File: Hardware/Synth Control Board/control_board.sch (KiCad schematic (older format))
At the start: 41 parts, among them J1 Conn_01x13, J2 Conn_01x03, J3 Conn_01x13, J4 Conn_01x13, J5 Conn_01x02, J6 Conn_01x13, J7 Conn_01x08, SW1 SW_DPDT_x2, SW10 SW_SPST, SW11 SW_SPST, SW12 SW_SPST, SW13 SW_SPST, SW2 SW_SPST, SW3 SW_SPST, SW4 SW_SPST, SW5 SW_SPST, SW6 SW_SPST, SW7 SW_SPST, SW8 SW_SPST, SW9 SW_SPST

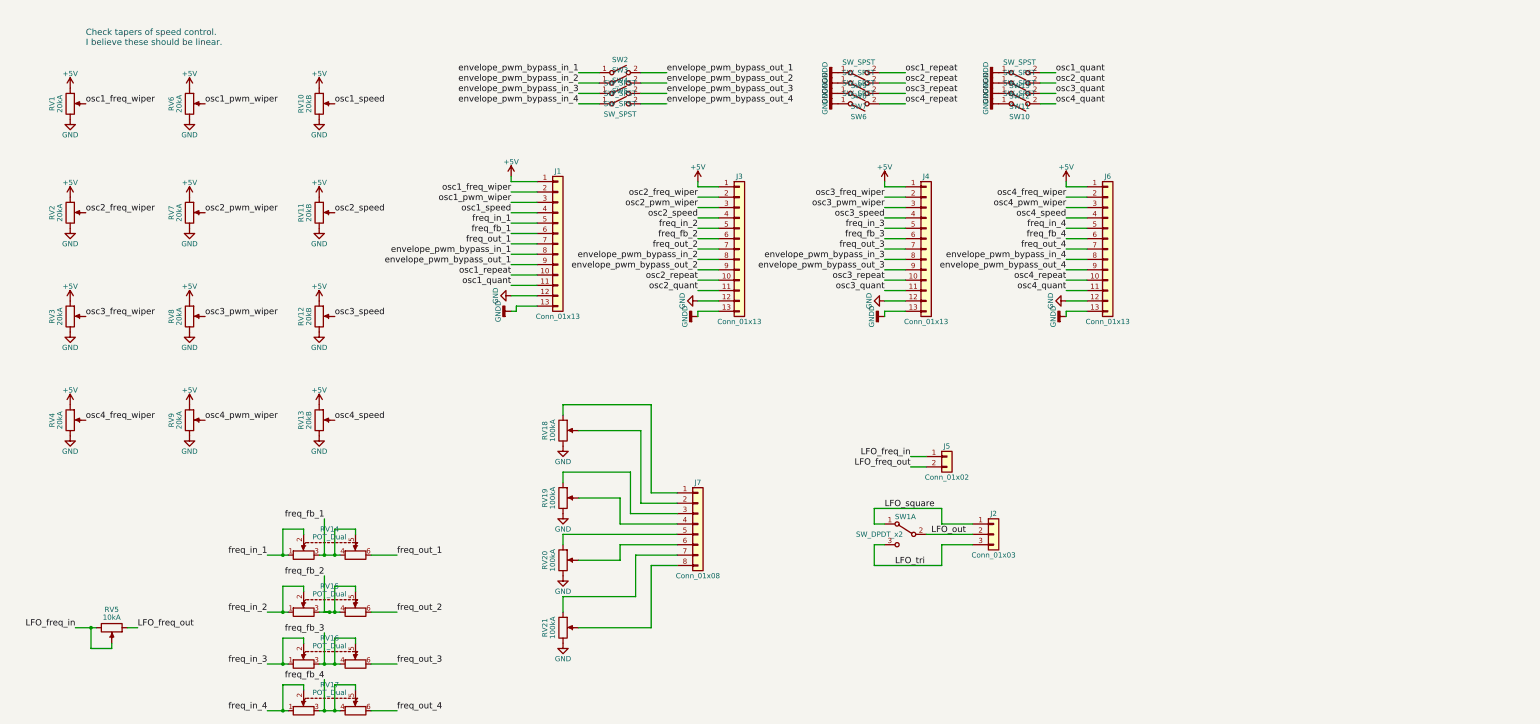
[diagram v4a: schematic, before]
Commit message: add LFO mod pots to control board and fix pot placement
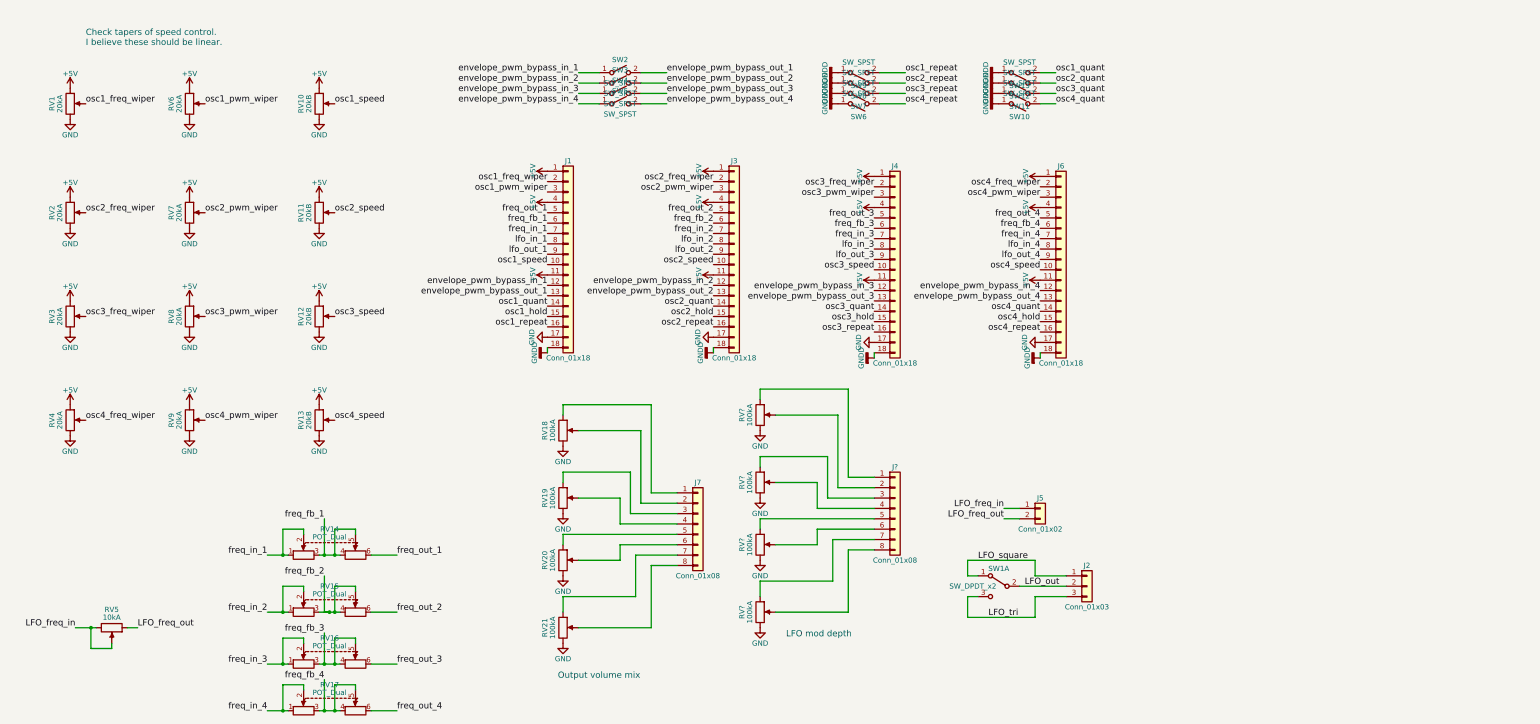
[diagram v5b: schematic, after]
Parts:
- removed J1, J3, J4, J6: Conn_01x13, Pin_Headers:Pin_Header_Straight_1x13_Pitch2.54mm, symbol Conn_01x13
- added J1, J3, J4, J6: Conn_01x18, Pin_Headers:Pin_Header_Straight_1x18_Pitch2.54mm, symbol Conn_01x18
- added J?: Conn_01x08, Pin_Headers:Pin_Header_Straight_1x08_Pitch2.54mm, symbol Conn_01x08
- added RV? (x4): 100kA, Potentiometers:Potentiometer_Bourns_PTV09A-1_Horizontal, symbol POT
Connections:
- net +5V: now also J1.1 (Pin_1), J1.11 (Pin_11), J1.4 (Pin_4), J3.1 (Pin_1), J3.11 (Pin_11), J3.4 (Pin_4), J4.1 (Pin_1), J4.11 (Pin_11), J4.4 (Pin_4), J6.1 (Pin_1), J6.11 (Pin_11), J6.4 (Pin_4)
- net GND: now also J1.17 (Pin_17), J3.17 (Pin_17), J4.17 (Pin_17), J6.17 (Pin_17), RV?.3, RV?.3, RV?.3, RV?.3
- net GNDD: now also J1.18 (Pin_18), J3.18 (Pin_18), J4.18 (Pin_18), J6.18 (Pin_18)
- net envelope_pwm_bypass_in_1: now also J1.12 (Pin_12)
- net envelope_pwm_bypass_in_2: now also J3.12 (Pin_12)
- net envelope_pwm_bypass_in_3: now also J4.12 (Pin_12)
- net envelope_pwm_bypass_in_4: now also J6.12 (Pin_12)
- net envelope_pwm_bypass_out_1: now also J1.13 (Pin_13)
- net envelope_pwm_bypass_out_2: now also J3.13 (Pin_13)
- net envelope_pwm_bypass_out_3: now also J4.13 (Pin_13)
- net envelope_pwm_bypass_out_4: now also J6.13 (Pin_13)
- net freq_fb_1: now also J1.6 (Pin_6)
- net freq_fb_2: now also J3.6 (Pin_6)
- net freq_fb_3: now also J4.6 (Pin_6)
- net freq_fb_4: now also J6.6 (Pin_6)
- net freq_in_1: now also J1.7 (Pin_7)
- net freq_in_2: now also J3.7 (Pin_7)
- net freq_in_3: now also J4.7 (Pin_7)
- net freq_in_4: now also J6.7 (Pin_7)
- net freq_out_1: now also J1.5 (Pin_5)
- net freq_out_2: now also J3.5 (Pin_5)
- net freq_out_3: now also J4.5 (Pin_5)
- net freq_out_4: now also J6.5 (Pin_5)
- net osc1_freq_wiper: now also J1.2 (Pin_2)
- net osc1_pwm_wiper: now also J1.3 (Pin_3)
- net osc1_quant: now also J1.14 (Pin_14)
- net osc1_repeat: now also J1.16 (Pin_16)
- net osc1_speed: now also J1.10 (Pin_10)
- net osc2_freq_wiper: now also J3.2 (Pin_2)
- net osc2_pwm_wiper: now also J3.3 (Pin_3)
- net osc2_quant: now also J3.14 (Pin_14)
- net osc2_repeat: now also J3.16 (Pin_16)
- net osc2_speed: now also J3.10 (Pin_10)
- net osc3_freq_wiper: now also J4.2 (Pin_2)
- net osc3_pwm_wiper: now also J4.3 (Pin_3)
- net osc3_quant: now also J4.14 (Pin_14)
- net osc3_repeat: now also J4.16 (Pin_16)
- net osc3_speed: now also J4.10 (Pin_10)
- net osc4_freq_wiper: now also J6.2 (Pin_2)
- net osc4_pwm_wiper: now also J6.3 (Pin_3)
- net osc4_quant: now also J6.14 (Pin_14)
- net osc4_repeat: now also J6.16 (Pin_16)
- net osc4_speed: now also J6.10 (Pin_10)
- new net: J?.1 (Pin_1), RV?.1
- new net: J?.2 (Pin_2), RV?.2
- new net: J?.3 (Pin_3), RV?.1
- new net: J?.4 (Pin_4), RV?.2
- new net: J?.5 (Pin_5), RV?.1
- new net: J?.6 (Pin_6), RV?.2
- new net: J?.7 (Pin_7), RV?.1
- new net: J?.8 (Pin_8), RV?.2
- new net lfo_in_1: J1.8 (Pin_8)
- new net lfo_in_2: J3.8 (Pin_8)
- new net lfo_in_3: J4.8 (Pin_8)
- new net lfo_in_4: J6.8 (Pin_8)
- new net lfo_out_1: J1.9 (Pin_9)
- new net lfo_out_2: J3.9 (Pin_9)
- new net lfo_out_3: J4.9 (Pin_9)
- new net lfo_out_4: J6.9 (Pin_9)
- new net osc1_hold: J1.15 (Pin_15)
- new net osc2_hold: J3.15 (Pin_15)
- new net osc3_hold: J4.15 (Pin_15)
- new net osc4_hold: J6.15 (Pin_15)
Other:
- note added: "LFO mod depth"
- note added: "Output volume mix"
- moved on the sheet: J2, J5, SW1A

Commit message: route traces to bypass caps on MCU. control board and connectors are WIP.
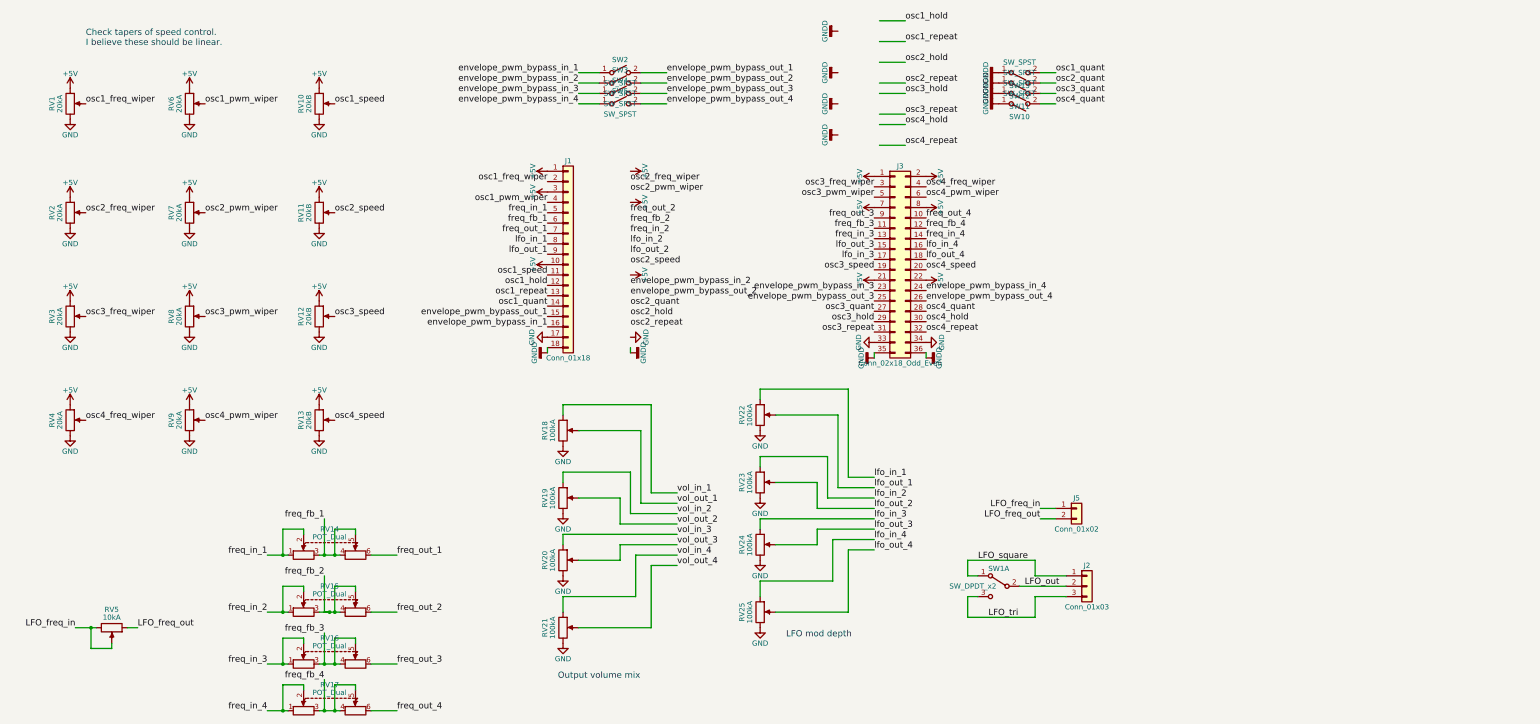
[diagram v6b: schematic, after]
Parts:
- removed J3, J4, J6: Conn_01x18, Pin_Headers:Pin_Header_Straight_1x18_Pitch2.54mm, symbol Conn_01x18
- removed J7, J?: Conn_01x08, Pin_Headers:Pin_Header_Straight_1x08_Pitch2.54mm, symbol Conn_01x08
- removed SW6, SW7, SW8, SW9: SW_SPST, SparkFun-Electromechanical:SWITCH-SPDT, symbol SW_SPST
- added J3: Conn_02x18_Odd_Even, Pin_Headers:Pin_Header_Straight_2x18_Pitch2.54mm, symbol Conn_02x18_Odd_Even
- gave numbers to parts that had none: 4
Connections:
- net labels added: vol_in_1, vol_in_2, vol_in_3, vol_in_4, vol_out_1, vol_out_2, vol_out_3, vol_out_4
- wire segments 131 -> 135
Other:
- moved on the sheet: J5

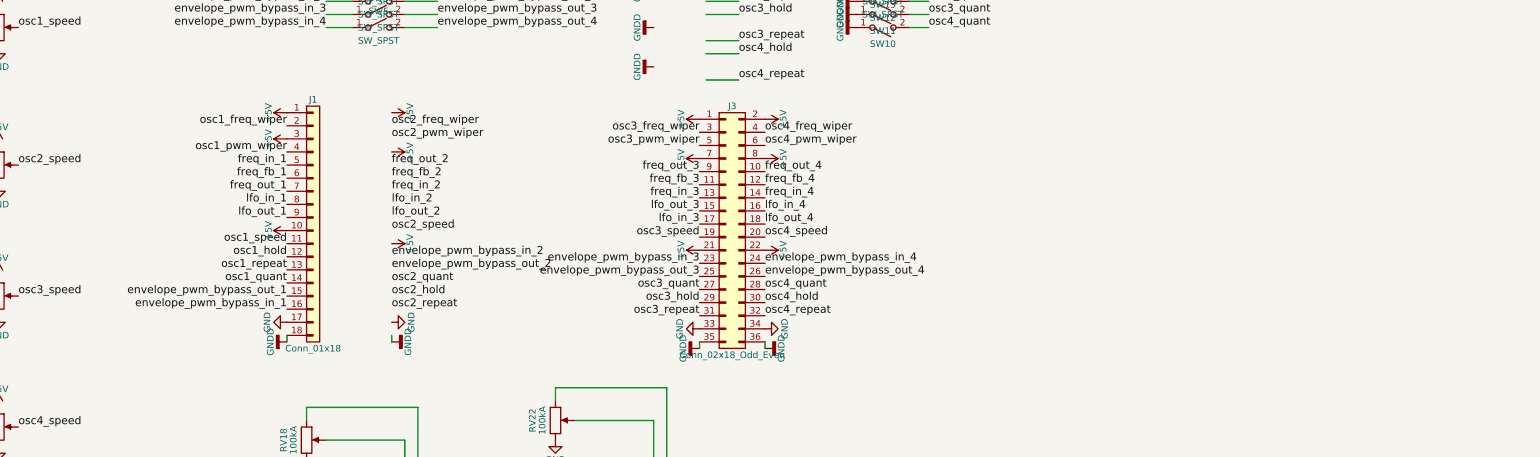
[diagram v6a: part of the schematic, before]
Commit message: route connectors on control board. Will add additional set of connectors for filter knobs to simplify routing.
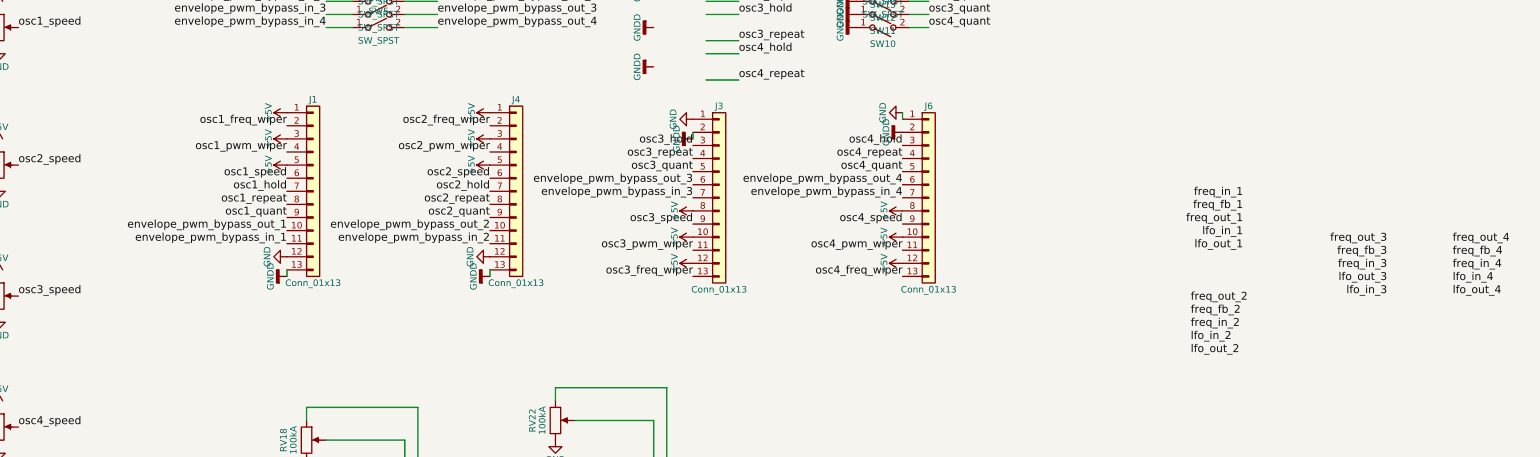
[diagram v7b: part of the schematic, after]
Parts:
- removed J1: Conn_01x18, Pin_Headers:Pin_Header_Straight_1x18_Pitch2.54mm, symbol Conn_01x18
- removed J3: Conn_02x18_Odd_Even, Pin_Headers:Pin_Header_Straight_2x18_Pitch2.54mm, symbol Conn_02x18_Odd_Even
- added J1, J3, J4, J6: Conn_01x13, Pin_Headers:Pin_Header_Straight_1x13_Pitch2.54mm, symbol Conn_01x13

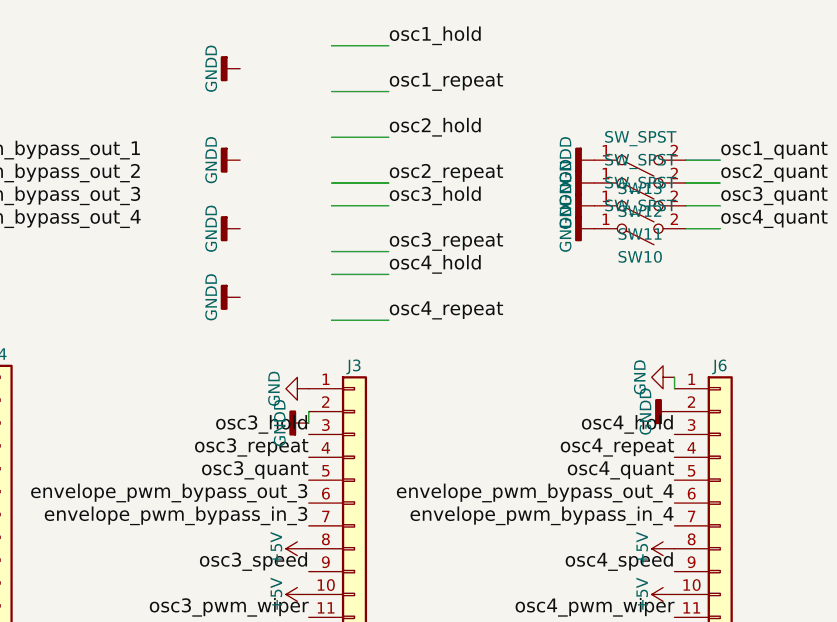
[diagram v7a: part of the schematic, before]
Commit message: fix SPDT hold/repeat switches on control board
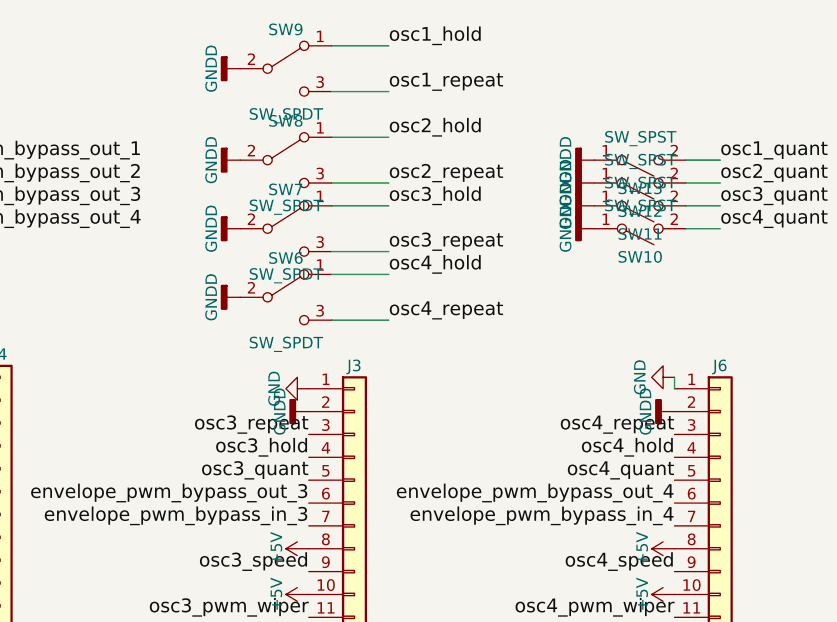
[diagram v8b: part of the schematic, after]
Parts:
- added SW6, SW7, SW8, SW9: SW_SPDT, SparkFun-Electromechanical:SWITCH-SPDT, symbol SW_SPDT
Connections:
- wire segments 135 -> 134
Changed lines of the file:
@@
 Text Label 8800 2500 2    60   ~ 0
 envelope_pwm_bypass_out_3
-Text Label 8800 2300 2    60   ~ 0
+Text Label 8800 2200 2    60   ~ 0
 osc3_repeat
 Text Label 8800 2400 2    60   ~ 0
@@
 L GNDD #PWR049
 U 1 1 5C6257E6
-P 8800 2150
-F 0 "#PWR049" H 8800 1900 50  0001 C CNN
-F 1 "GNDD" H 8800 2025 50  0000 C CNN
-F 2 "" H 8800 2150 50  0001 C CNN
-F 3 "" H 8800 2150 50  0001 C CNN
-	1    8800 2150
+P 8800 2100
+F 0 "#PWR049" H 8800 1850 50  0001 C CNN
+F 1 "GNDD" H 8800 1975 50  0000 C CNN
+F 2 "" H 8800 2100 50  0001 C CNN
+F 3 "" H 8800 2100 50  0001 C CNN
+	1    8800 2100
 	0    1    -1   0
 $EndComp
@@
 	0    -1   -1   0
 $EndComp
-Text Label 8800 2200 2    60   ~ 0
+Text Label 8800 2300 2    60   ~ 0
 osc3_hold
-Wire Wire Line
-	8800 2100 8800 2150
 Text Label 10400 3200 2    60   ~ 0
 osc4_freq_wiper
@@
 Text Label 10400 2500 2    60   ~ 0
 envelope_pwm_bypass_out_4
-Text Label 10400 2300 2    60   ~ 0
+Text Label 10400 2200 2    60   ~ 0
 osc4_repeat
 Text Label 10400 2400 2    60   ~ 0
@@
 	0    -1   -1   0
 $EndComp
-Text Label 10400 2200 2    60   ~ 0
+Text Label 10400 2300 2    60   ~ 0
 osc4_hold
 $Comp
@@
 Wire Wire Line
 	10400 2000 10400 1950
+$Comp
+L SW_SPDT SW9
+U 1 1 5C6395CA
+P 8700 600
+F 0 "SW9" H 8700 770 50  0000 C CNN
+F 1 "SW_SPDT" H 8700 400 50  0000 C CNN
+F 2 "SparkFun-Electromechanical:SWITCH-SPDT" H 8700 600 50  0001 C CNN
+F 3 "" H 8700 600 50  0001 C CNN
+	1    8700 600
+	1    0    0    -1
+$EndComp
+$Comp
+L SW_SPDT SW8
+U 1 1 5C63968E
+P 8700 1000
+F 0 "SW8" H 8700 1170 50  0000 C CNN
+F 1 "SW_SPDT" H 8700 800 50  0000 C CNN
+F 2 "SparkFun-Electromechanical:SWITCH-SPDT" H 8700 1000 50  0001 C CNN
+F 3 "" H 8700 1000 50  0001 C CNN
+	1    8700 1000
+	1    0    0    -1
+$EndComp
+$Comp
+L SW_SPDT SW7
+U 1 1 5C639730
+P 8700 1300
+F 0 "SW7" H 8700 1470 50  0000 C CNN
+F 1 "SW_SPDT" H 8700 1100 50  0000 C CNN
+F 2 "SparkFun-Electromechanical:SWITCH-SPDT" H 8700 1300 50  0001 C CNN
+F 3 "" H 8700 1300 50  0001 C CNN
+	1    8700 1300
+	1    0    0    -1
+$EndComp
+$Comp
+L SW_SPDT SW6
+U 1 1 5C6397C9
+P 8700 1600
+F 0 "SW6" H 8700 1770 50  0000 C CNN
+F 1 "SW_SPDT" H 8700 1400 50  0000 C CNN
+F 2 "SparkFun-Electromechanical:SWITCH-SPDT" H 8700 1600 50  0001 C CNN
+F 3 "" H 8700 1600 50  0001 C CNN
+	1    8700 1600
+	1    0    0    -1
+$EndComp
 $EndSCHEMATC
